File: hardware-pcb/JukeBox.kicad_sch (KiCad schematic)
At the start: 77 parts, among them J1 USB4105-GF-A, J2 AudioJack4_Ground, Q1 Q_NPN_ECB, SW1 SW_SPST, SW10 SW_SPST, SW11 SW_SPST, SW12 SW_SPST, SW2 SW_SPST, SW3 SW_SPST, SW4 SW_SPST, SW5 SW_SPST, SW6 SW_SPST, SW7 SW_SPST, SW8 SW_SPST, SW9 SW_SPST, U1 NCP1117-3.3_SOT223, U2 W25Q128JVS, U3 RP2040, U4 st7789v, Y1 ECS-120-20-33-AEL-TR

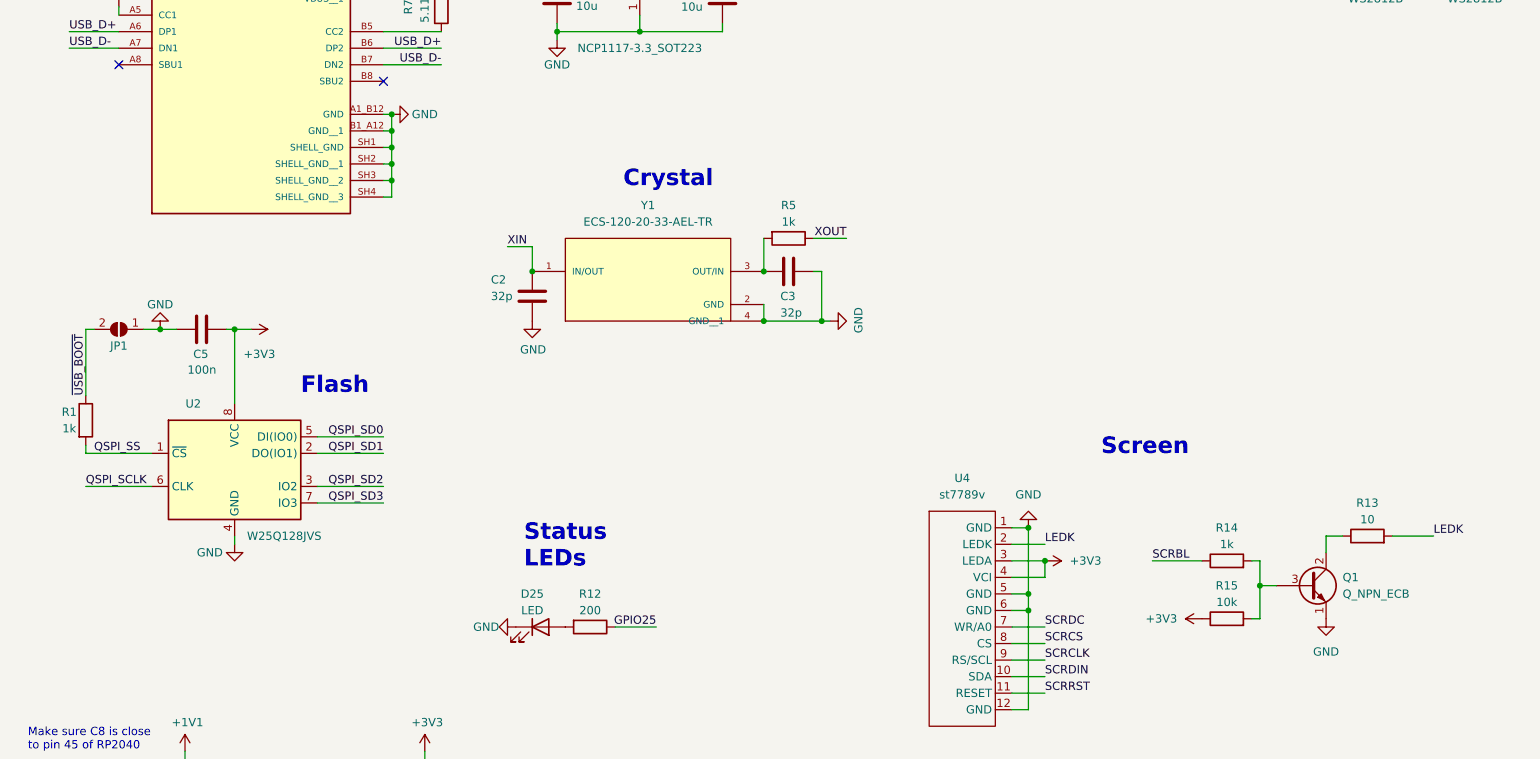
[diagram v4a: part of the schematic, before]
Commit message: update flash chip, fix backlight transistor, adjust some holes for io, update readme for hardware
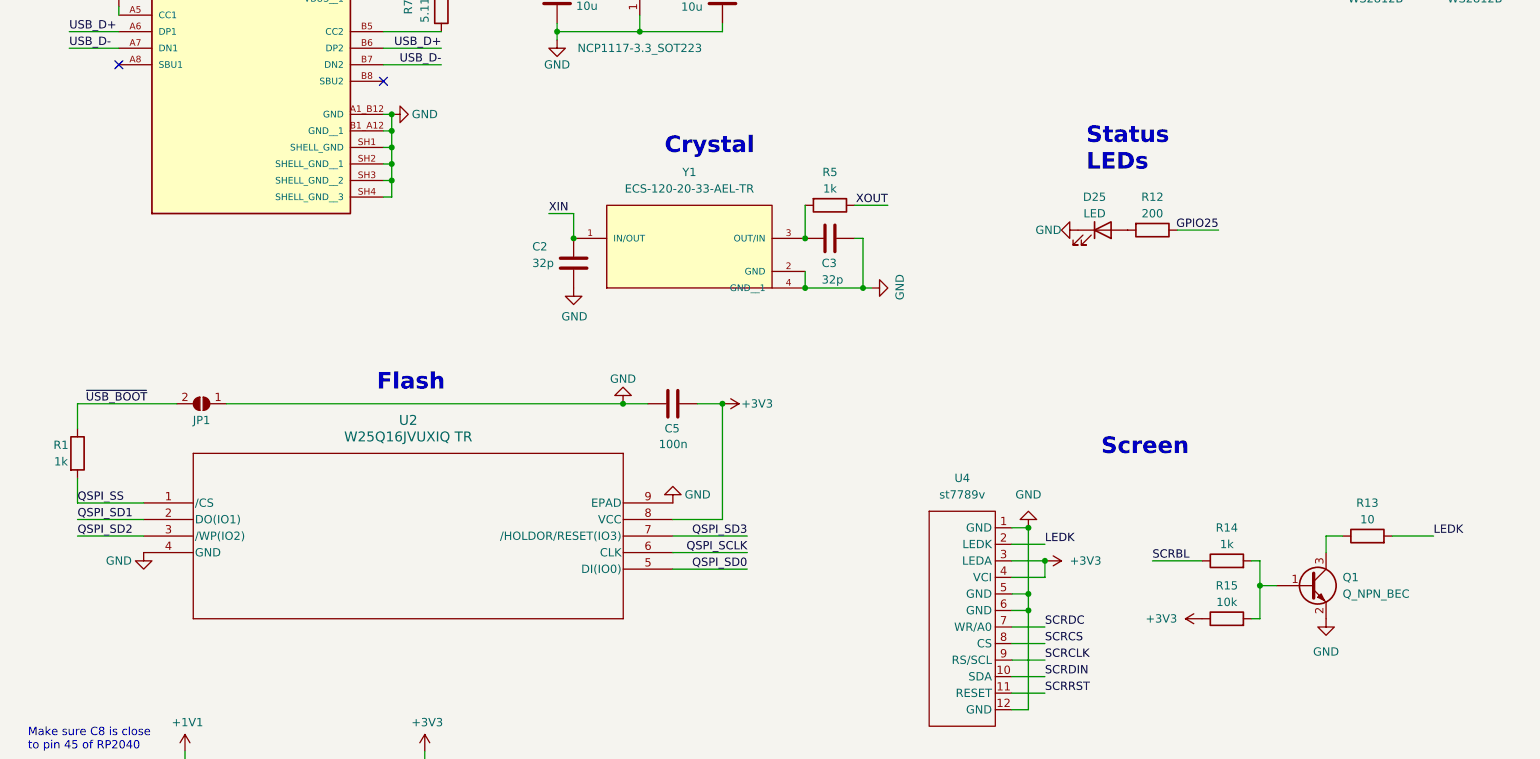
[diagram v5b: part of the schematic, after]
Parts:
- removed Q1: Q_NPN_ECB, Package_TO_SOT_SMD:SOT-23, symbol Device:Q_NPN_ECB
- removed U2: W25Q128JVS, Package_SO:SOIC-8_3.9x4.9mm_P1.27mm, symbol Memory_Flash:W25Q128JVS
- added Q1: Q_NPN_BEC, Package_TO_SOT_SMD:SOT-23, symbol Device:Q_NPN_BEC
- added U2: W25Q16JVUXIQ TR, JukeBox:USON-8_UX_2x3x0p6_WIN, symbol W25Q16JVUXIQ-TR:W25Q16JVUXIQ_TR
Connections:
- net +3V3: now also U2.8 (VCC)
- net GND: now also Q1.2 (E), U2.4 (GND), U2.9 (EPAD)
- net QSPI_SCLK: now also U2.6 (CLK)
- net QSPI_SD0: now also U2.5 (DI(IO0))
- net QSPI_SD1: now also U2.2 (DO(IO1))
- net QSPI_SD2: now also U2.3 (/WP(IO2))
- net QSPI_SD3: now also U2.7 (/HOLDOR/RESET(IO3))
- net QSPI_SS: now also U2.1 (/CS)
- net at R13.1: now also Q1.3 (C)
- net at R14.2, R15.2: now also Q1.1 (B)
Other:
- moved on the sheet: C2, C3, C5, D25, R12, R5, Y1

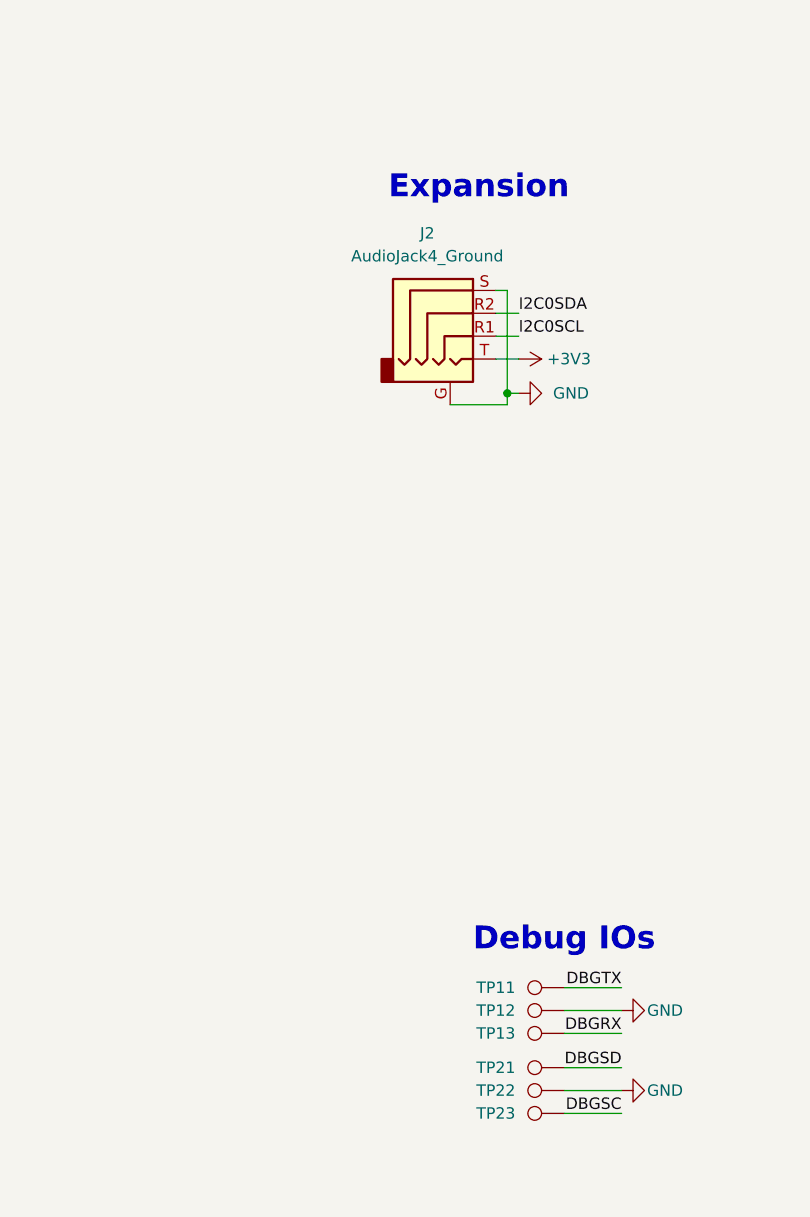
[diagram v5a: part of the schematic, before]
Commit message: remove headphone jack, switch to test pads, use 2020 leds and rearrange, move usb port
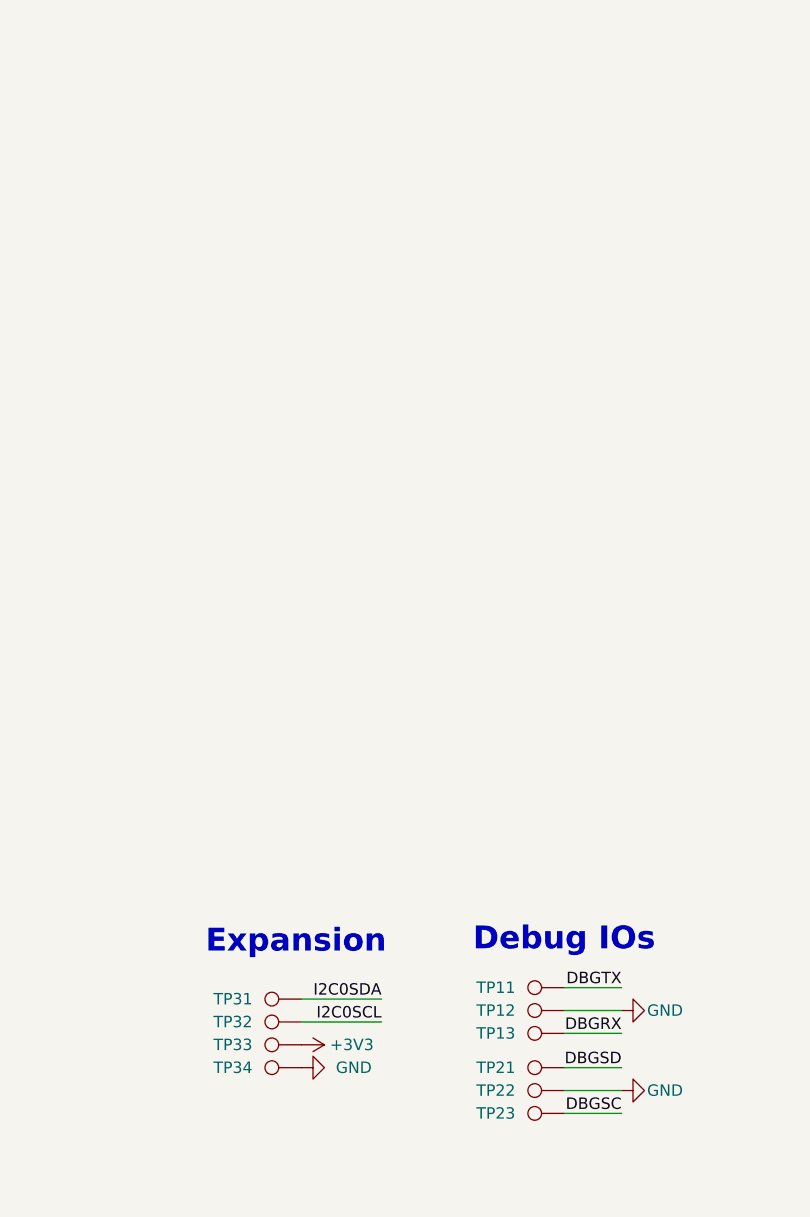
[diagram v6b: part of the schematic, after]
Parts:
- removed J2: AudioJack4_Ground, Connector_Audio:Jack_3.5mm_PJ320E_Horizontal, symbol Connector_Audio:AudioJack4_Ground
- added TP31, TP32, TP33, TP34: TestPoint, TestPoint:TestPoint_Pad_D1.5mm, symbol Connector:TestPoint
- D13, D14, D15, D16, D17, D18, D19, D20, D21, D22, D23, D24: footprint LED_SMD:LED_WS2812B_PLCC4_5.0x5.0mm_P3.2mm -> LED_SMD:LED_WS2812B-2020_PLCC4_2.0x2.0mm
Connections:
- net +3V3: now also TP33.1
- net GND: now also TP34.1
- net GPIO4: now also TP31.1
- net GPIO5: now also TP32.1

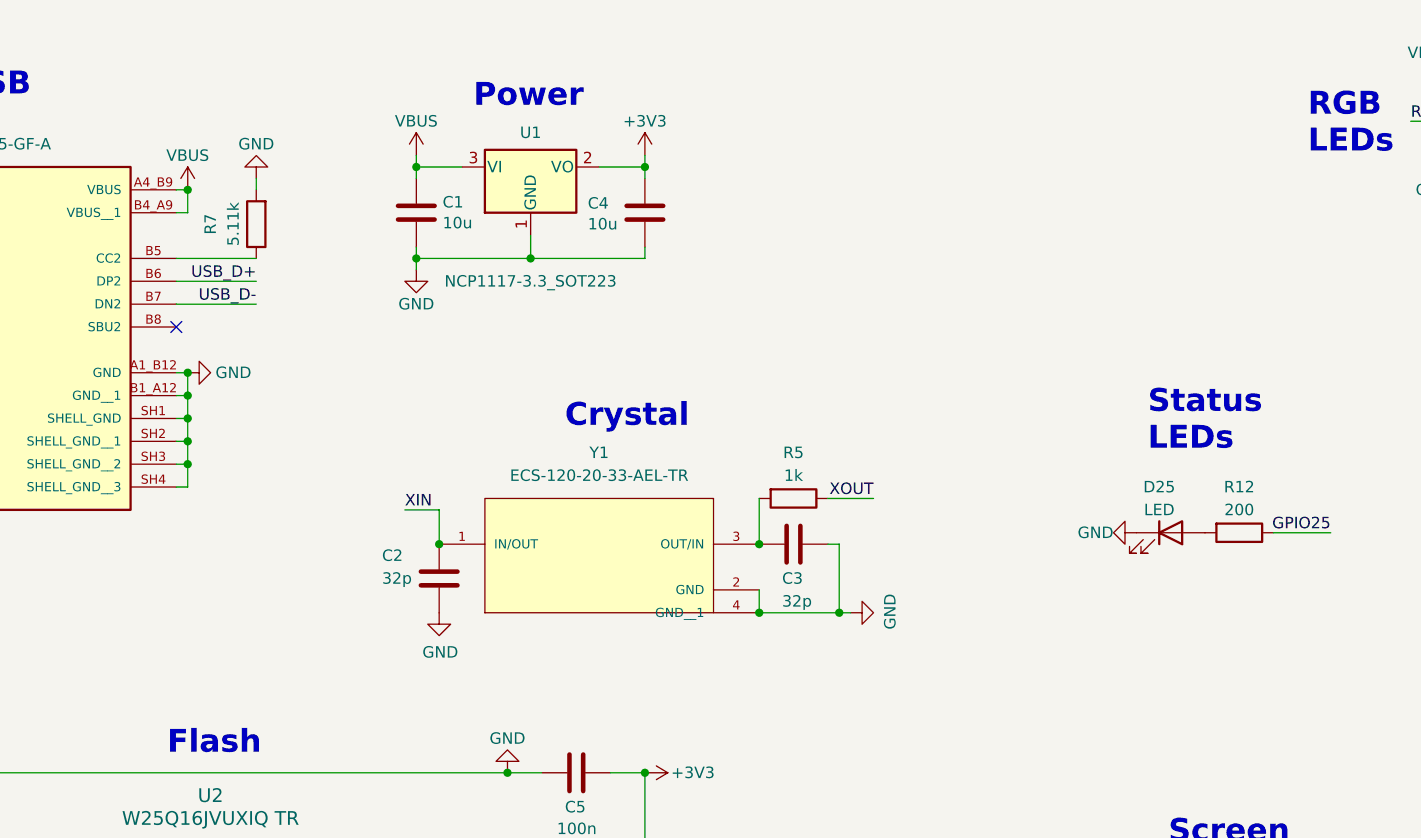
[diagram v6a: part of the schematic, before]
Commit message: add board id to lcd, other misc minor updates
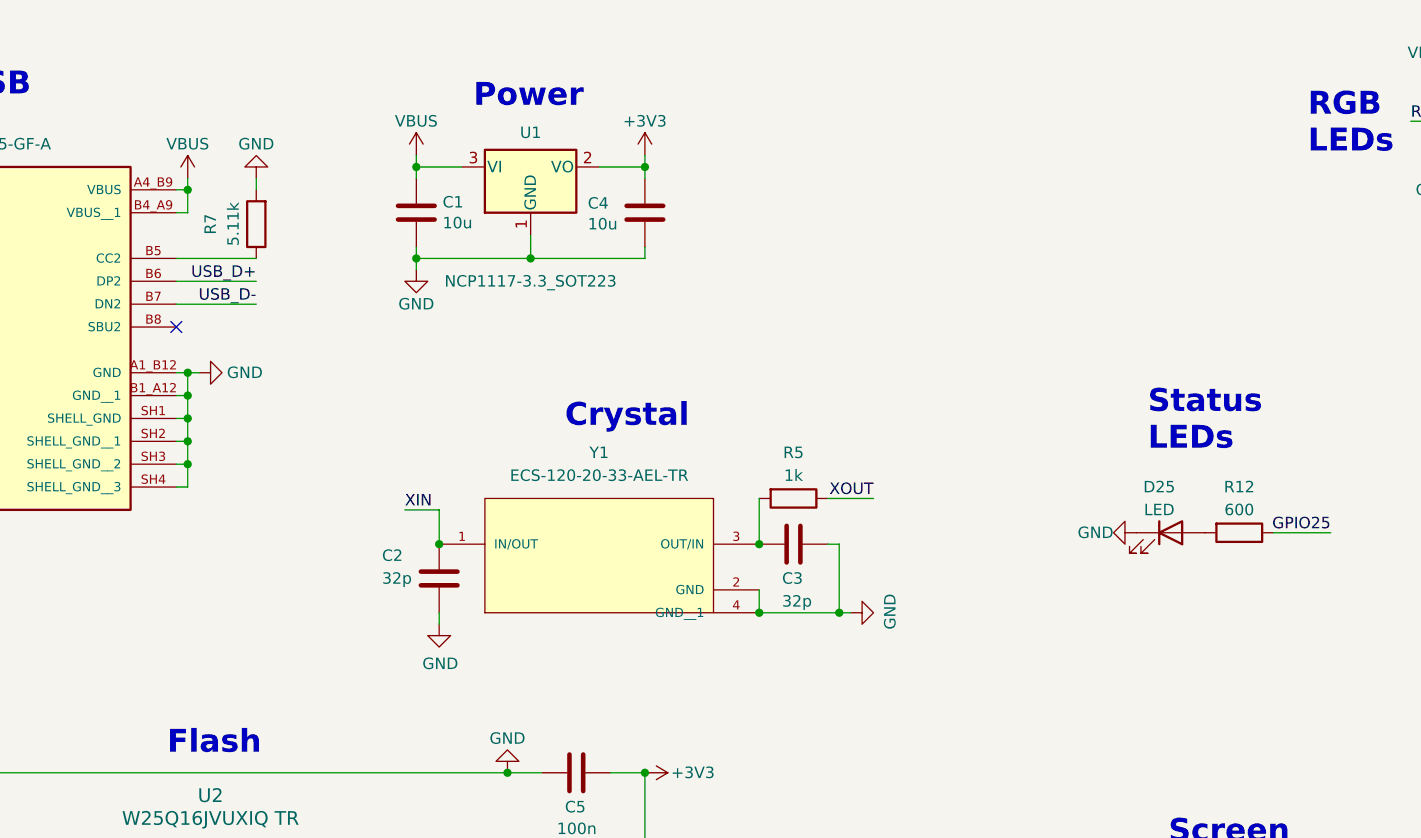
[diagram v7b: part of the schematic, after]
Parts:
- R12: value 200 -> 600
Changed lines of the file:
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@@
 	(wire
 		(pts
+			(xy 71.12 33.02) (xy 71.12 34.29)
+		)
+		(stroke
+			(width 0)
+			(type default)
+		)
+	)
+	(wire
+		(pts
 			(xy 91.44 246.38) (xy 106.68 246.38)
 		)
@@
 	(wire
 		(pts
+			(xy 99.06 82.55) (xy 99.06 81.28)
+		)
+		(stroke
+			(width 0)
+			(type default)
+		)
+	)
+	(wire
+		(pts
 			(xy 166.37 118.11) (xy 168.91 118.11)
 		)
@@
 	(wire
 		(pts
+			(xy 72.39 54.61) (xy 71.12 54.61)
+		)
+		(stroke
+			(width 0)
+			(type default)
+		)
+	)
+	(wire
+		(pts
 			(xy 203.2 264.16) (xy 196.85 264.16)
 		)
@@
 	(symbol
 		(lib_id "power:GND")
-		(at 99.06 81.28 0)
+		(at 99.06 82.55 0)
 		(unit 1)
 		(exclude_from_sim no)
@@
 		(dnp no)
 		(property "Reference" "#PWR06"
-			(at 99.06 87.63 0)
+			(at 99.06 88.9 0)
 			(effects
 				(font
@@
 		)
 		(property "Value" "GND"
-			(at 99.187 85.6742 0)
+			(at 99.187 86.9442 0)
 			(effects
 				(font
@@
 		)
 		(property "Footprint" ""
-			(at 99.06 81.28 0)
+			(at 99.06 82.55 0)
 			(effects
 				(font
@@
 		)
 		(property "Datasheet" ""
-			(at 99.06 81.28 0)
+			(at 99.06 82.55 0)
 			(effects
 				(font
@@
 		)
 		(property "Description" ""
-			(at 99.06 81.28 0)
+			(at 99.06 82.55 0)
 			(effects
 				(font
@@
 			)
 		)
-		(property "Value" "200"
+		(property "Value" "600"
 			(at 187.96 69.85 90)
 			(effects
@@
 	(symbol
 		(lib_id "power:VBUS")
-		(at 71.12 34.29 0)
+		(at 71.12 33.02 0)
 		(unit 1)
 		(exclude_from_sim no)
@@
 		(dnp no)
 		(property "Reference" "#PWR0120"
-			(at 71.12 38.1 0)
+			(at 71.12 36.83 0)
 			(effects
 				(font
@@
 		)
 		(property "Value" "VBUS"
-			(at 71.12 30.48 0)
+			(at 71.12 29.21 0)
 			(effects
 				(font
@@
 		)
 		(property "Footprint" ""
-			(at 71.12 34.29 0)
+			(at 71.12 33.02 0)
 			(effects
 				(font
@@
 		)
 		(property "Datasheet" ""
-			(at 71.12 34.29 0)
+			(at 71.12 33.02 0)
 			(effects
 				(font
@@
 		)
 		(property "Description" ""
-			(at 71.12 34.29 0)
+			(at 71.12 33.02 0)
 			(effects
 				(font
@@
 	(symbol
 		(lib_id "power:GND")
-		(at 71.12 54.61 90)
+		(at 72.39 54.61 90)
 		(unit 1)
 		(exclude_from_sim no)
@@
 		(dnp no)
 		(property "Reference" "#PWR0109"
-			(at 77.47 54.61 0)
+			(at 78.74 54.61 0)
 			(effects
 				(font
@@
 		)
 		(property "Value" "GND"
-			(at 76.2 54.61 90)
+			(at 77.47 54.61 90)
 			(effects
 				(font
@@
 		)
 		(property "Footprint" ""
-			(at 71.12 54.61 0)
+			(at 72.39 54.61 0)
 			(effects
 				(font
@@
 		)
 		(property "Datasheet" ""
-			(at 71.12 54.61 0)
+			(at 72.39 54.61 0)
 			(effects
 				(font
@@
 		)
 		(property "Description" ""
-			(at 71.12 54.61 0)
+			(at 72.39 54.61 0)
 			(effects
 				(font
